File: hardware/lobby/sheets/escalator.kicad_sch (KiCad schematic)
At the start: 2 parts

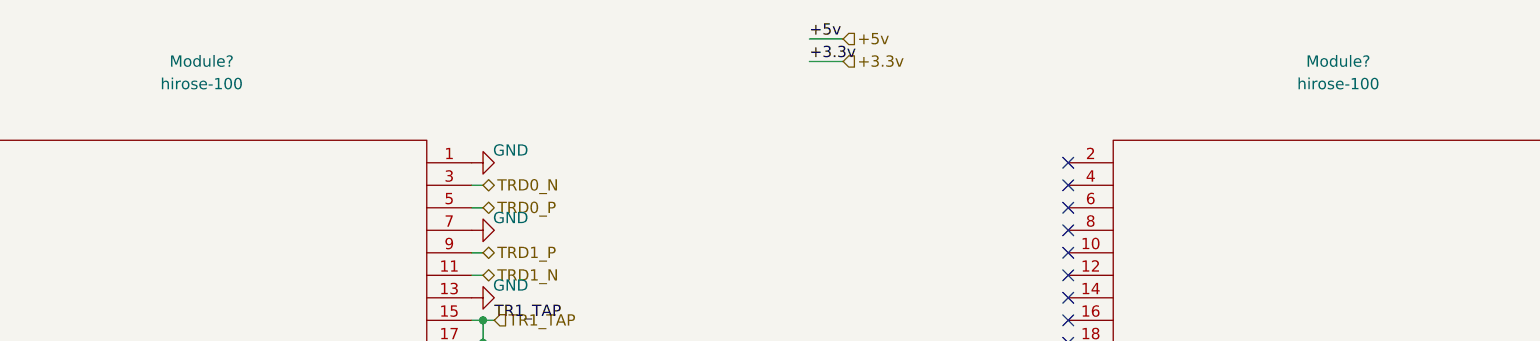
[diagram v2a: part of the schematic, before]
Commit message: work abroad
did some light planning for the lobby board while on vacation. now ready for final placement + routing
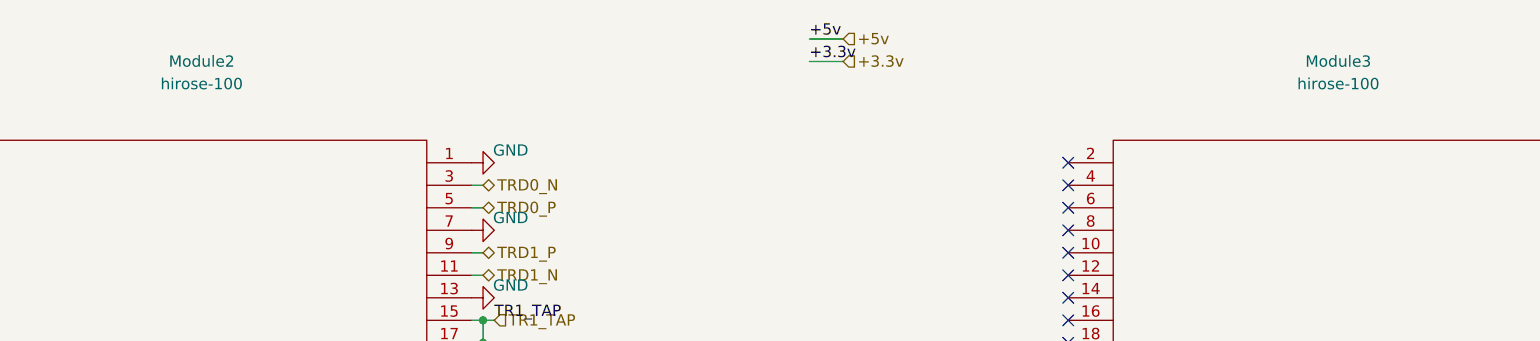
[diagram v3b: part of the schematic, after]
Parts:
- gave numbers to parts that had none: 2
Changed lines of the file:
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@@
   (symbol (lib_id "power:GND") (at 54.61 30.48 270) (unit 1)
     (in_bom yes) (on_board yes)
-    (property "Reference" "#PWR?" (id 0) (at 48.26 30.48 0)
+    (property "Reference" "#PWR069" (id 0) (at 48.26 30.48 0)
       (effects (font (size 1.27 1.27)) hide)
     )
@@
   (symbol (lib_id "power:GND") (at 54.61 38.1 270) (unit 1)
     (in_bom yes) (on_board yes)
-    (property "Reference" "#PWR?" (id 0) (at 48.26 38.1 0)
+    (property "Reference" "#PWR070" (id 0) (at 48.26 38.1 0)
       (effects (font (size 1.27 1.27)) hide)
     )
@@
   (symbol (lib_id "power:GND") (at 54.61 45.72 270) (unit 1)
     (in_bom yes) (on_board yes)
-    (property "Reference" "#PWR?" (id 0) (at 48.26 45.72 0)
+    (property "Reference" "#PWR071" (id 0) (at 48.26 45.72 0)
       (effects (font (size 1.27 1.27)) hide)
     )
@@
   (symbol (lib_id "power:GND") (at 54.61 55.88 270) (unit 1)
     (in_bom yes) (on_board yes)
-    (property "Reference" "#PWR?" (id 0) (at 48.26 55.88 0)
+    (property "Reference" "#PWR072" (id 0) (at 48.26 55.88 0)
       (effects (font (size 1.27 1.27)) hide)
     )
@@
   (symbol (lib_id "power:GND") (at 54.61 66.04 270) (unit 1)
     (in_bom yes) (on_board yes)
-    (property "Reference" "#PWR?" (id 0) (at 48.26 66.04 0)
+    (property "Reference" "#PWR073" (id 0) (at 48.26 66.04 0)
       (effects (font (size 1.27 1.27)) hide)
     )
@@
   (symbol (lib_id "power:GND") (at 54.61 86.36 270) (unit 1)
     (in_bom yes) (on_board yes)
-    (property "Reference" "#PWR?" (id 0) (at 48.26 86.36 0)
+    (property "Reference" "#PWR074" (id 0) (at 48.26 86.36 0)
       (effects (font (size 1.27 1.27)) hide)
     )
@@
   (symbol (lib_id "power:GND") (at 54.61 93.98 270) (unit 1)
     (in_bom yes) (on_board yes)
-    (property "Reference" "#PWR?" (id 0) (at 48.26 93.98 0)
+    (property "Reference" "#PWR075" (id 0) (at 48.26 93.98 0)
       (effects (font (size 1.27 1.27)) hide)
     )
@@
   (symbol (lib_id "power:GND") (at 54.61 106.68 270) (unit 1)
     (in_bom yes) (on_board yes)
-    (property "Reference" "#PWR?" (id 0) (at 48.26 106.68 0)
+    (property "Reference" "#PWR076" (id 0) (at 48.26 106.68 0)
       (effects (font (size 1.27 1.27)) hide)
     )
@@
   (symbol (lib_id "power:GND") (at 54.61 109.22 270) (unit 1)
     (in_bom yes) (on_board yes)
-    (property "Reference" "#PWR?" (id 0) (at 48.26 109.22 0)
+    (property "Reference" "#PWR077" (id 0) (at 48.26 109.22 0)
       (effects (font (size 1.27 1.27)) hide)
     )
@@
   (symbol (lib_id "power:GND") (at 54.61 111.76 270) (unit 1)
     (in_bom yes) (on_board yes)
-    (property "Reference" "#PWR?" (id 0) (at 48.26 111.76 0)
+    (property "Reference" "#PWR078" (id 0) (at 48.26 111.76 0)
       (effects (font (size 1.27 1.27)) hide)
     )
@@
   (symbol (lib_id "power:GND") (at 54.61 124.46 270) (unit 1)
     (in_bom yes) (on_board yes)
-    (property "Reference" "#PWR?" (id 0) (at 48.26 124.46 0)
+    (property "Reference" "#PWR079" (id 0) (at 48.26 124.46 0)
       (effects (font (size 1.27 1.27)) hide)
     )
@@
   (symbol (lib_id "power:GND") (at 54.61 132.08 270) (unit 1)
     (in_bom yes) (on_board yes)
-    (property "Reference" "#PWR?" (id 0) (at 48.26 132.08 0)
+    (property "Reference" "#PWR080" (id 0) (at 48.26 132.08 0)
       (effects (font (size 1.27 1.27)) hide)
     )
@@
   (symbol (lib_id "power:GND") (at 54.61 139.7 270) (unit 1)
     (in_bom yes) (on_board yes)
-    (property "Reference" "#PWR?" (id 0) (at 48.26 139.7 0)
+    (property "Reference" "#PWR081" (id 0) (at 48.26 139.7 0)
       (effects (font (size 1.27 1.27)) hide)
     )
@@
   (symbol (lib_id "power:GND") (at 54.61 147.32 270) (unit 1)
     (in_bom yes) (on_board yes)
-    (property "Reference" "#PWR?" (id 0) (at 48.26 147.32 0)
+    (property "Reference" "#PWR082" (id 0) (at 48.26 147.32 0)
       (effects (font (size 1.27 1.27)) hide)
     )
@@
   (symbol (lib_id "power:GND") (at 54.61 154.94 270) (unit 1)
     (in_bom yes) (on_board yes)
-    (property "Reference" "#PWR?" (id 0) (at 48.26 154.94 0)
+    (property "Reference" "#PWR083" (id 0) (at 48.26 154.94 0)
       (effects (font (size 1.27 1.27)) hide)
     )
@@
   (symbol (lib_id "power:GND") (at 115.57 30.48 90) (unit 1)
     (in_bom yes) (on_board yes)
-    (property "Reference" "#PWR?" (id 0) (at 121.92 30.48 0)
+    (property "Reference" "#PWR084" (id 0) (at 121.92 30.48 0)
       (effects (font (size 1.27 1.27)) hide)
     )
@@
   (symbol (lib_id "power:GND") (at 115.57 38.1 90) (unit 1)
     (in_bom yes) (on_board yes)
-    (property "Reference" "#PWR?" (id 0) (at 121.92 38.1 0)
+    (property "Reference" "#PWR085" (id 0) (at 121.92 38.1 0)
       (effects (font (size 1.27 1.27)) hide)
     )
@@
   (symbol (lib_id "power:GND") (at 115.57 45.72 90) (unit 1)
     (in_bom yes) (on_board yes)
-    (property "Reference" "#PWR?" (id 0) (at 121.92 45.72 0)
+    (property "Reference" "#PWR086" (id 0) (at 121.92 45.72 0)
       (effects (font (size 1.27 1.27)) hide)
     )
@@
   (symbol (lib_id "power:GND") (at 115.57 55.88 90) (unit 1)
     (in_bom yes) (on_board yes)
-    (property "Reference" "#PWR?" (id 0) (at 121.92 55.88 0)
+    (property "Reference" "#PWR087" (id 0) (at 121.92 55.88 0)
       (effects (font (size 1.27 1.27)) hide)
     )
@@
   (symbol (lib_id "power:GND") (at 115.57 66.04 90) (unit 1)
     (in_bom yes) (on_board yes)
-    (property "Reference" "#PWR?" (id 0) (at 121.92 66.04 0)
+    (property "Reference" "#PWR088" (id 0) (at 121.92 66.04 0)
       (effects (font (size 1.27 1.27)) hide)
     )
@@
   (symbol (lib_id "power:GND") (at 115.57 86.36 90) (unit 1)
     (in_bom yes) (on_board yes)
-    (property "Reference" "#PWR?" (id 0) (at 121.92 86.36 0)
+    (property "Reference" "#PWR089" (id 0) (at 121.92 86.36 0)
       (effects (font (size 1.27 1.27)) hide)
     )
@@
   (symbol (lib_id "power:GND") (at 115.57 88.9 90) (unit 1)
     (in_bom yes) (on_board yes)
-    (property "Reference" "#PWR?" (id 0) (at 121.92 88.9 0)
+    (property "Reference" "#PWR090" (id 0) (at 121.92 88.9 0)
       (effects (font (size 1.27 1.27)) hide)
     )
@@
   (symbol (lib_id "power:GND") (at 115.57 96.52 90) (unit 1)
     (in_bom yes) (on_board yes)
-    (property "Reference" "#PWR?" (id 0) (at 121.92 96.52 0)
+    (property "Reference" "#PWR091" (id 0) (at 121.92 96.52 0)
       (effects (font (size 1.27 1.27)) hide)
     )
@@
   (symbol (lib_id "power:GND") (at 115.57 104.14 90) (unit 1)
     (in_bom yes) (on_board yes)
-    (property "Reference" "#PWR?" (id 0) (at 121.92 104.14 0)
+    (property "Reference" "#PWR092" (id 0) (at 121.92 104.14 0)
       (effects (font (size 1.27 1.27)) hide)
     )
@@
   (symbol (lib_id "power:GND") (at 115.57 111.76 90) (unit 1)
     (in_bom yes) (on_board yes)
-    (property "Reference" "#PWR?" (id 0) (at 121.92 111.76 0)
+    (property "Reference" "#PWR093" (id 0) (at 121.92 111.76 0)
       (effects (font (size 1.27 1.27)) hide)
     )
@@
   (symbol (lib_id "power:GND") (at 115.57 124.46 90) (mirror x) (unit 1)
     (in_bom yes) (on_board yes)
-    (property "Reference" "#PWR?" (id 0) (at 121.92 124.46 0)
+    (property "Reference" "#PWR094" (id 0) (at 121.92 124.46 0)
       (effects (font (size 1.27 1.27)) hide)
     )
@@
   (symbol (lib_id "power:GND") (at 115.57 132.08 90) (unit 1)
     (in_bom yes) (on_board yes)
-    (property "Reference" "#PWR?" (id 0) (at 121.92 132.08 0)
+    (property "Reference" "#PWR095" (id 0) (at 121.92 132.08 0)
       (effects (font (size 1.27 1.27)) hide)
     )
@@
   (symbol (lib_id "power:GND") (at 115.57 139.7 90) (unit 1)
     (in_bom yes) (on_board yes)
-    (property "Reference" "#PWR?" (id 0) (at 121.92 139.7 0)
+    (property "Reference" "#PWR096" (id 0) (at 121.92 139.7 0)
       (effects (font (size 1.27 1.27)) hide)
     )
@@
   (symbol (lib_id "power:GND") (at 115.57 147.32 90) (unit 1)
     (in_bom yes) (on_board yes)
-    (property "Reference" "#PWR?" (id 0) (at 121.92 147.32 0)
+    (property "Reference" "#PWR097" (id 0) (at 121.92 147.32 0)
       (effects (font (size 1.27 1.27)) hide)
     )
@@
   (symbol (lib_id "power:GND") (at 115.57 154.94 90) (unit 1)
     (in_bom yes) (on_board yes)
-    (property "Reference" "#PWR?" (id 0) (at 121.92 154.94 0)
+    (property "Reference" "#PWR098" (id 0) (at 121.92 154.94 0)
       (effects (font (size 1.27 1.27)) hide)
     )
@@
   (symbol (lib_id "cm4crypto:hirose-100") (at 87.63 91.44 0) (unit 1)
     (in_bom yes) (on_board yes) (fields_autoplaced)
-    (property "Reference" "Module?" (id 0) (at 85.09 19.05 0))
+    (property "Reference" "Module2" (id 0) (at 85.09 19.05 0))
     (property "Value" "hirose-100" (id 1) (at 85.09 21.59 0))
     (property "Footprint" "cm4crypto:DF40C-100DP-0.4V(51)" (id 2) (at 95.25 212.09 0)
@@
   (symbol (lib_id "cm4crypto:hirose-100") (at 215.9 91.44 0) (unit 1)
     (in_bom yes) (on_board yes) (fields_autoplaced)
-    (property "Reference" "Module?" (id 0) (at 213.36 19.05 0))
+    (property "Reference" "Module3" (id 0) (at 213.36 19.05 0))
     (property "Value" "hirose-100" (id 1) (at 213.36 21.59 0))
     (property "Footprint" "cm4crypto:DF40C-100DP-0.4V(51)" (id 2) (at 223.52 212.09 0)
